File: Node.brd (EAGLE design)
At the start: 38.1 x 38.1 mm, 72 parts, among them J1 AVR_SPI_PRG_6NS, J2 M04X2, Q1 PMR280UN, Q2 PMR280UN, Q3 PMR280UN, U1 ATMEGA32U4, U2 BLUETOOTH-RN41", U4 L3GD20, U5 LTC3554, U6 LSM303DLHC, U9 RCLAMP0502A, X1 USBSMD

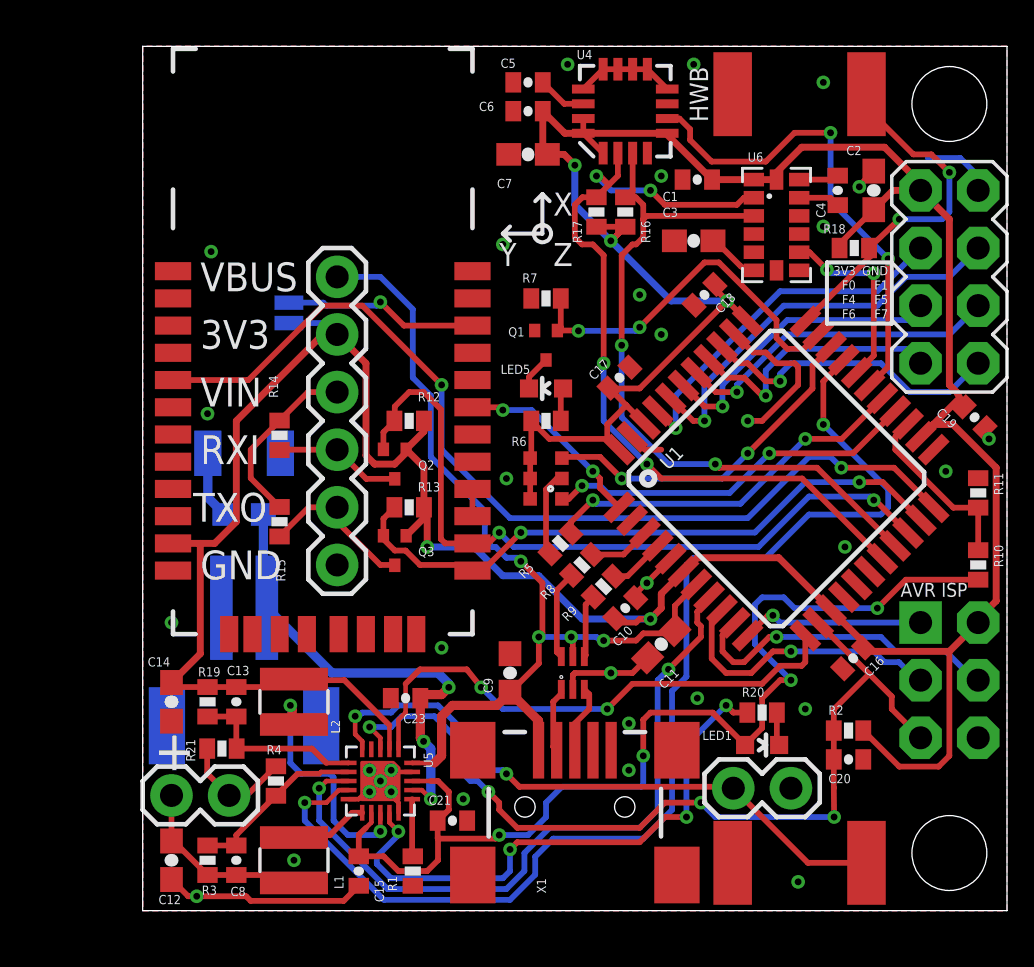
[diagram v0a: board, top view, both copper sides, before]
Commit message: cleanup for rev3 and use ltc3553
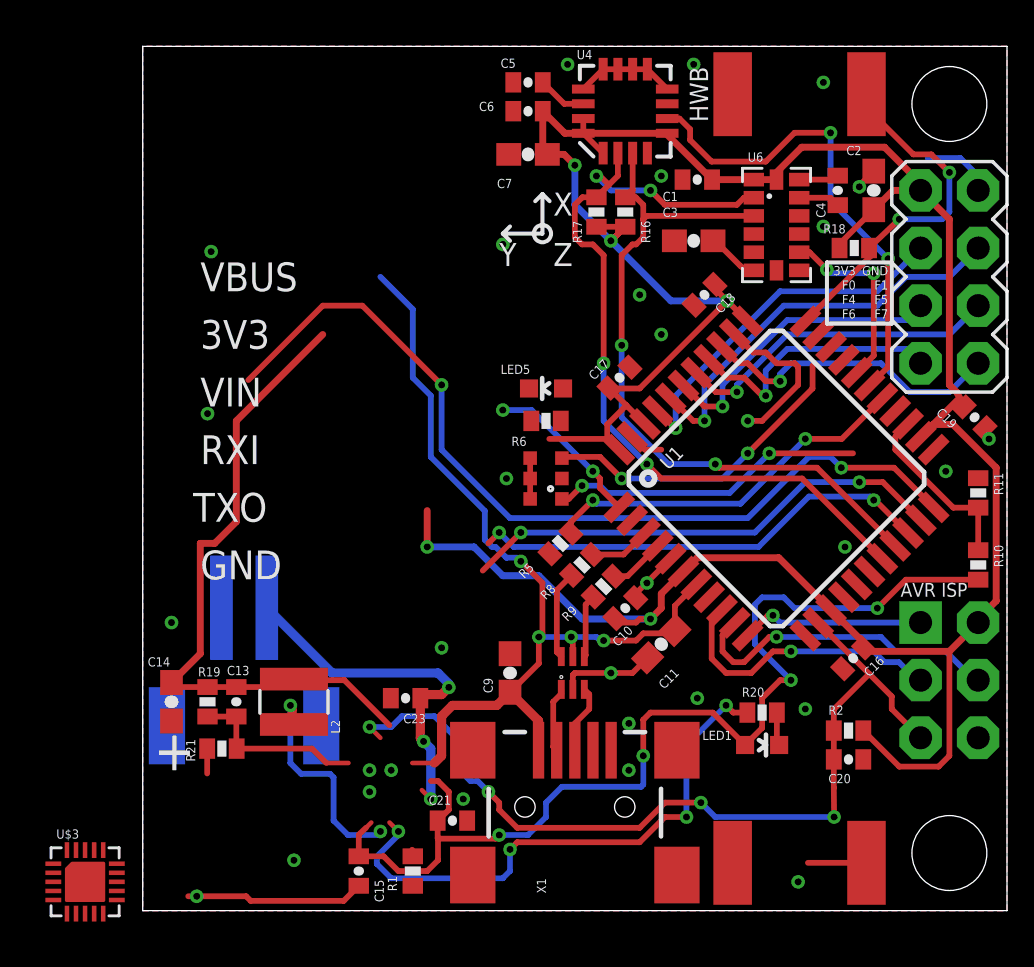
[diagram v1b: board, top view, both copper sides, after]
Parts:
- removed C12: 10uF, SparkFun:0603-CAP
- removed C22: 100uF, SparkFun:1210
- removed C8: 10pF, SparkFun:0402-CAP
- removed JP1: ON, SparkFun-Connectors:1X02
- removed JP2: UART, SparkFun:1X06
- removed JP3: 3V3, SparkFun-Connectors:1X02
- removed L1: 4.7uH, adjacent-reality:VLS30
- removed Q1, Q2, Q3: PMR280UN, adjacent-reality:SOT416
- removed R12, R13, R14, R15: 4.7k, SparkFun:0402-RES
- removed R22: 0.3, SparkFun:0603-RES
- removed R3: 2.05M, SparkFun:0402-RES
- removed R4: 649k, SparkFun:0402-RES
- removed R7: 1M, SparkFun:0402-RES
- removed SJ1: SOLDERJUMPERNO, SparkFun:SJ_2S-NO
- removed U2: BLUETOOTH-RN41", adjacent-reality:RN41
- removed U5: LTC3554, adjacent-reality:QFN20-3X3
- added U$3: LTC3553, adjacent-reality:QFN20-3X3
- R1: value 1.5k -> 7.5k
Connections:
- removed net HPWR: U1.12, U5.1
- removed net N$14: SJ1.1, U2.22
- removed net N$19: C12.1, C8.1, JP3.1, L1.2, R3.2
- removed net N$20: LED5.C, Q1.3
- removed net N$22: Q1.1, R7.2, U1.32
- removed net N$23: L1.1, U5.11
- removed net N$31: C8.2, R3.1, R4.2, U5.7
- removed net N$36: C22.1, R22.1
- removed net N$9 (its old number): U2.15, U2.16
- removed net PWR_ON1: U1.30, U5.9
- removed net PWR_ON2: U1.8, U5.8
- removed net RX_I: JP2.4, Q2.3, R14.1
- removed net TX_O: JP2.5, Q3.3, R15.1
- removed net VIN: JP2.3, R14.2, R15.2
- new net BUCK_ON: U$3.1
- new net N$10: LED5.C, R6.1
- new net STBY: U$3.6
- net +3V3: now also LED5.A; no longer JP2.2, Q2.1, Q3.1, R12.2, R13.2, R6.2, SJ1.2, U2.11, U5.2
- net GND: now also U$3.15, U$3.19, U$3.2, U$3.21, U$3.5; no longer C12.2, C22.2, JP1.2, JP2.6, JP3.2, Q1.2, R4.1, R7.1, U2.1, U2.12, U2.20, U2.28, U2.29, U2.3, U2.4, U5.10, U5.15, U5.19, U5.21
- net N$1: now also U$3.11, U$3.12, U$3.18; no longer U5.12, U5.18
- net N$12: now also U1.32; no longer U1.31
- net N$16: now also U$3.14; no longer U5.14
- net N$17: now also U1.30; no longer U1.26
- net N$2: now also U$3.16; no longer U5.16
- net N$27: now also U$3.13; no longer U5.13
- net N$29: now also U$3.17; no longer R22.2, U5.17
- net N$37: now also U$3.8; no longer U5.6
- net N$4: now also R6.2, U1.31; no longer LED5.A, R6.1
- net N$8: no longer JP1.1, U5.5
- net RBT: no longer U2.5
- net RESET: no longer U5.3
- net RX: no longer Q2.2, R12.1, U2.14
- net SBT: no longer U2.19
- net TX: no longer Q3.2, R13.1, U2.13
- net VBUS: now also U$3.20; no longer JP2.1, U5.20
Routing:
- net PWR_ON1: track 51.8 -> 0.00 mm, vias 2 -> 0
- net PWR_ON2: track 31.4 -> 0.00 mm, vias 2 -> 0
- net N$8: track 27.9 -> 2.58 mm, vias 2 -> 0
- net HPWR: track 23.7 -> 0.00 mm, vias 2 -> 0
- net +3V3: track 180.0 -> 157.6 mm
- net N$22: track 16.5 -> 0.00 mm, vias 2 -> 0
- net RX: track 33.2 -> 20.5 mm
- net GND: track 43.1 -> 33.1 mm, vias 33 -> 31
- net N$14: track 8.64 -> 0.00 mm, vias 1 -> 0
- net N$19: track 8.17 -> 0.00 mm
- net VIN: track 7.92 -> 0.00 mm
- net N$31: track 7.85 -> 0.00 mm
- net TX_O: track 7.04 -> 0.00 mm
- net TX: track 28.2 -> 21.6 mm
- net RX_I: track 5.62 -> 0.00 mm
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
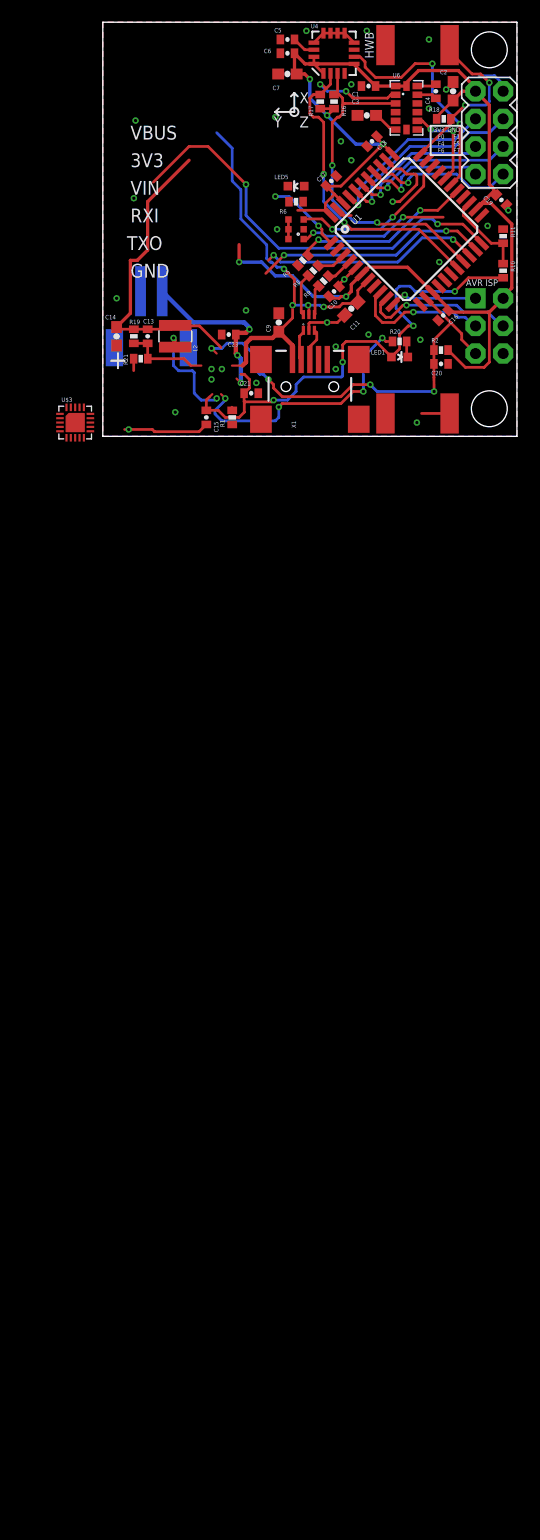
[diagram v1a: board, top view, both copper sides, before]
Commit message: add header and crystal
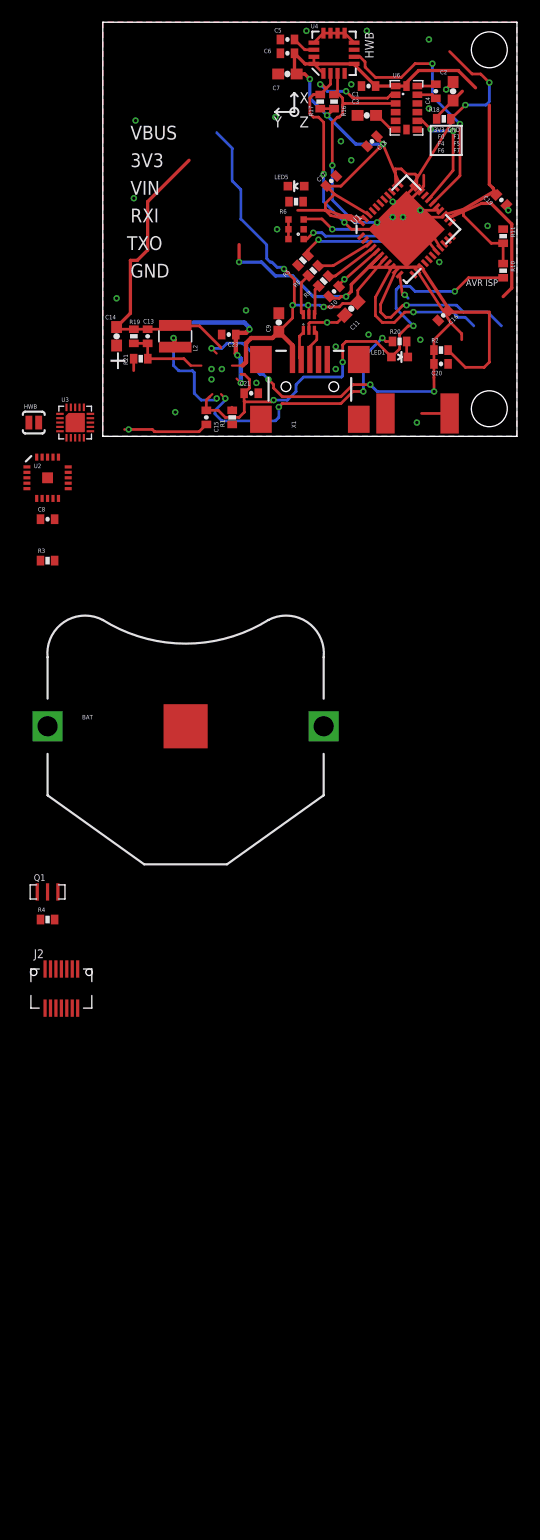
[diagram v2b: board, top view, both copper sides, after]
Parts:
- removed J1: AVR_SPI_PRG_6NS, SparkFun:2X3-NS
- added C8: 33nF, SparkFun:0402-CAP
- added Q1: 16MHz, adjacent-reality:PRQC
- added R3: 22k, SparkFun:0402-RES
- added R4: 1M, SparkFun:0402-RES
- added U2: NRF24L01SMD, SparkFun-RF:QFN20
- BAT: value JST -> (none); device SparkFun:JST-2-SMD -> SparkFun-Electromechanical:BATTCON_245MM_PTH
- HWB: value KSS -> SOLDERJUMPERNO; device adjacent-reality:KSS -> SparkFun-Passives:SJ_2S-NO
- J2: value M04X2 -> DF12A3.0-14DS; device SparkFun:2X4 -> adjacent-reality:DF12A3.0-14DS
- U1: value ATMEGA32U4 -> ATMEGA32U4QFN; device adjacent-reality:TQFP44 -> adjacent-reality:QFN-44
- moved J2 88.0 mm to (-3.81, -50.8), turned to 0 degrees
- moved HWB 49.5 mm to (-6.35, 1.27), turned to 0 degrees
- moved BAT 36.5 mm to (7.62, -26.7), flipped to the top, turned to 0 degrees
- renumbered U$3 to U3
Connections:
- removed net N$28: J2.1, U1.36
- removed net N$30: J2.2, U1.37
- removed net N$32: J2.3, U1.38
- removed net N$33: J2.4, U1.39
- removed net N$34: J2.5, U1.40
- removed net N$35: J2.6, U1.41
- removed net RBT: U1.22
- removed net SBT: U1.1
- new net A0: J2.9, U1.41
- new net A1: J2.10, U1.40
- new net A4: J2.11, U1.39
- new net A5: J2.12, U1.38
- new net A6: J2.13, U1.37
- new net A7: J2.14, U1.36
- new net CE: U1.1, U2.1
- new net N$11: C8.1, U2.19
- new net N$14: R3.2, U2.16
- new net N$19: Q1.P$1, R4.1, U2.9
- new net N$20: Q1.P$3, R4.2, U2.10
- new net PCINT7: U1.12, U2.6
- new net SS: U1.8, U2.2
- new net VDD_PA: U2.11
- net +3V3: now also J2.2, U2.15, U2.18, U2.7; no longer J1.2, J2.8
- net BUCK_ON: now also U1.22
- net GND: now also BAT.2, C8.2, HWB.1, J2.6, Q1.P$2, R3.1, U2.0, U2.14, U2.17, U2.20, U2.8; no longer BAT.1, HWB.P$2, J1.6, J2.7
- net HWB: now also HWB.2; no longer HWB.P$1
- net MISO: now also J2.1, U2.5; no longer J1.1
- net MOSI: now also J2.4, U2.4; no longer J1.4
- net N$29: now also BAT.3; no longer BAT.2
- net RESET: now also J2.5; no longer J1.5
- net RX: now also J2.7
- net SCK: now also J2.3, U2.3; no longer J1.3
- net STBY: now also U1.26
- net TX: now also J2.8
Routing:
- net RBT: track 39.2 -> 0.00 mm, vias 2 -> 0
- net TX: track 21.6 -> 0.00 mm, vias 2 -> 0
- net RX: track 20.5 -> 0.00 mm, vias 2 -> 0
- net N$34: track 18.1 -> 0.00 mm, vias 1 -> 0
- net N$35: track 16.0 -> 0.00 mm, vias 1 -> 0
- net N$32: track 14.5 -> 0.00 mm, vias 1 -> 0
- net +3V3: track 157.6 -> 171.9 mm
- net N$28: track 13.5 -> 0.00 mm, vias 1 -> 0
- net N$33: track 13.2 -> 0.00 mm, vias 1 -> 0
- net N$30: track 11.7 -> 0.00 mm, vias 1 -> 0
- net SBT: track 7.34 -> 0.00 mm, vias 2 -> 0
- net MISO: track 8.13 -> 2.54 mm
- net N$29: track 16.4 -> 12.2 mm
- net N$15: track 2.71 -> 5.21 mm
- net MOSI: track 14.2 -> 16.7 mm
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
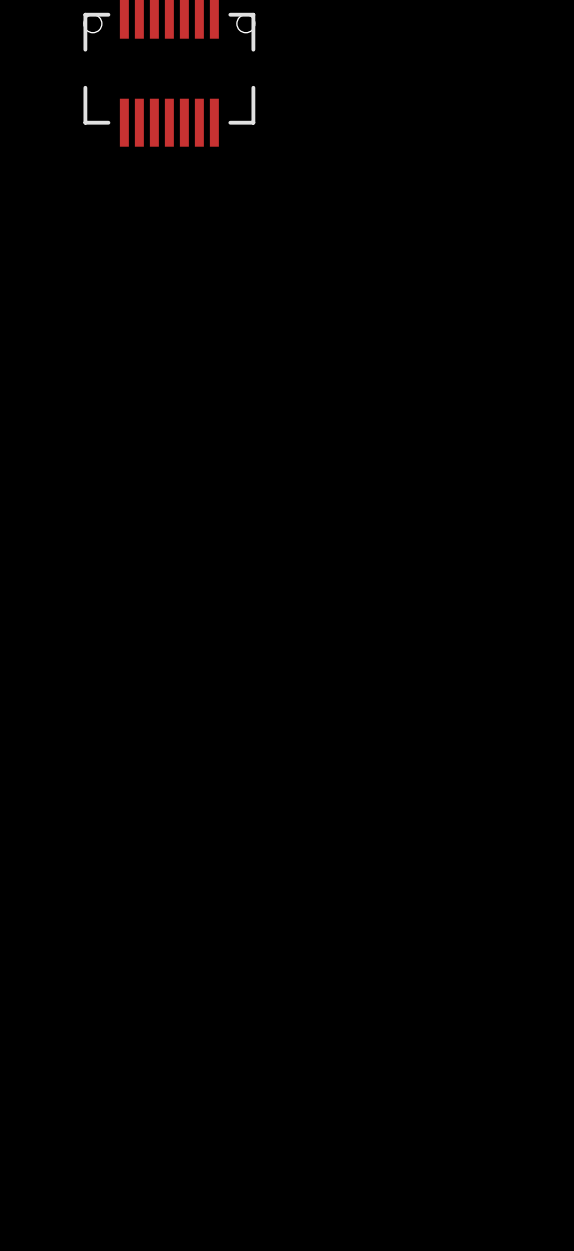
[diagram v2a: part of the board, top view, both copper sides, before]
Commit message: balun for nrf24l01
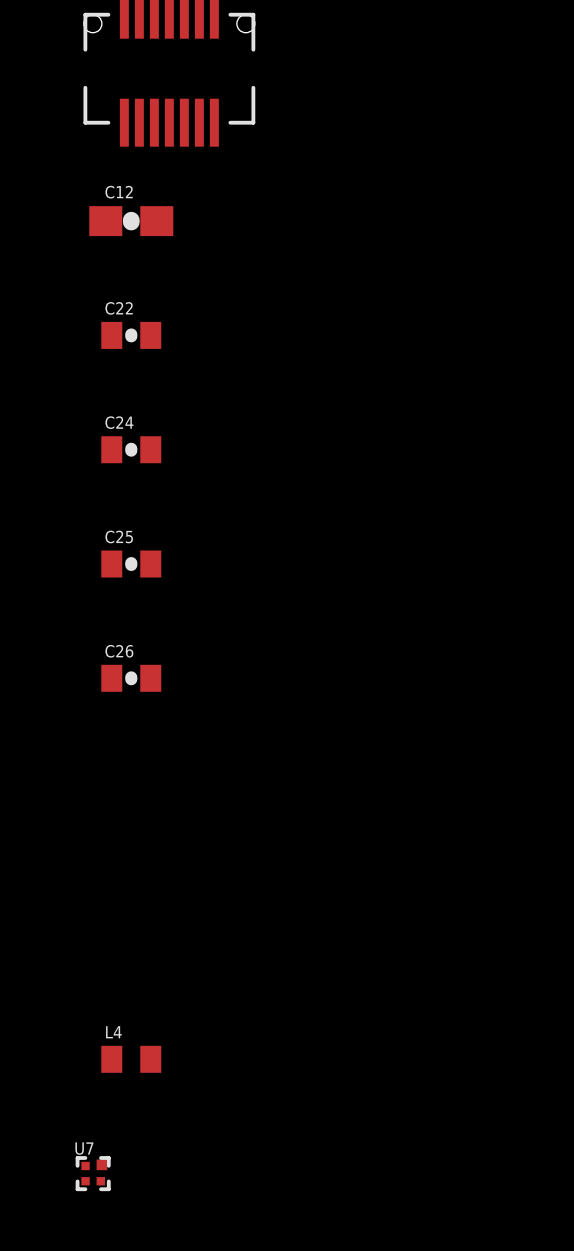
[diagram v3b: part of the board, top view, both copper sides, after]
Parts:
- added C12: 10uF, SparkFun:0603-CAP
- added C22: 10nF, SparkFun:0402-CAP
- added C24: 1nF, SparkFun:0402-CAP
- added C25: 2.2nF, SparkFun:0402-CAP
- added C26: 4.7pF, SparkFun:0402-CAP
- added L4: 3.9nH, adjacent-reality:C0402
- added U7: BD2425NNRF0404, adjacent-reality:BD2425NNRF
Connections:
- removed net VDD_PA: U2.11
- new net N$21: U2.13, U7.3
- new net N$22: U2.12, U7.4
- new net N$23: C25.1, C26.1, U2.11, U7.1
- new net N$28: L4.1, U7.2
- new net VSS: U2.0
- net +3V3: now also C12.1, C22.1, C24.1
- net GND: now also C12.2, C22.2, C24.2, C25.2, C26.2; no longer U2.0

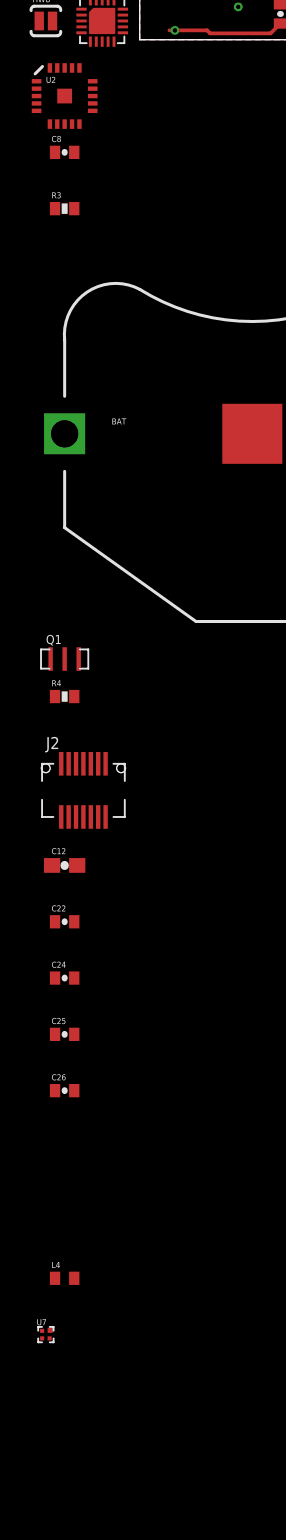
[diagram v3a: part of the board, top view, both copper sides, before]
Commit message: add the antenna
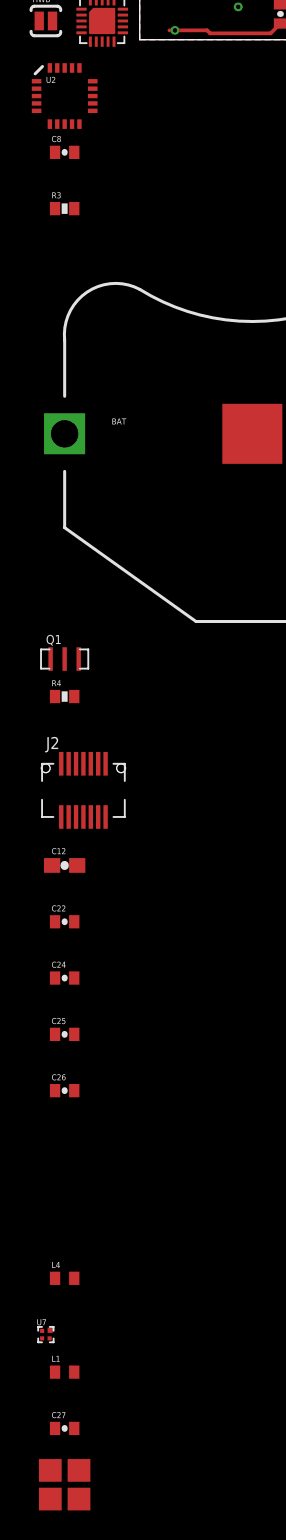
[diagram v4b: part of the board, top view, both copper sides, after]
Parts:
- added C27: TBD, SparkFun:0402-CAP
- added L1: TBD, adjacent-reality:C0402
- added RF: ANTENNA2MOLEX, adjacent-reality:MOLEX2.4SMD
- U2: value NRF24L01SMD -> NRF24L01NOPAD; device SparkFun-RF:QFN20 -> adjacent-reality:QFN20-NOPAD
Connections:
- removed net VSS: U2.0
- new net N$30: L1.2, RF.FEED
- new net N$31: C27.1, L1.1, L4.2
- net GND: now also C27.2
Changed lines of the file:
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@@
 <element name="U3" library="adjacent-reality" package="QFN20-3X3" value="LTC3553" x="-2.54" y="1.27"/>
 <element name="HWB" library="SparkFun-Passives" package="SJ_2S-NO" value="SOLDERJUMPERNO" x="-6.35" y="1.27"/>
-<element name="U2" library="SparkFun-RF" package="QFN20" value="NRF24L01SMD" x="-5.08" y="-3.81"/>
+<element name="U2" library="adjacent-reality" package="QFN20-NOPAD" value="NRF24L01NOPAD" x="-5.08" y="-3.81"/>
 <element name="C8" library="SparkFun" package="0402-CAP" value="33nF" x="-5.08" y="-7.62"/>
 <element name="R3" library="SparkFun" package="0402-RES" value="22k" x="-5.08" y="-11.43"/>
@@
 <element name="L4" library="adjacent-reality" package="C0402" value="3.9nH" x="-5.08" y="-83.82"/>
 <element name="U7" library="adjacent-reality" package="BD2425NNRF" value="BD2425NNRF0404" x="-6.35" y="-87.63"/>
+<element name="L1" library="adjacent-reality" package="C0402" value="TBD" x="-5.08" y="-90.17"/>
+<element name="C27" library="SparkFun" package="0402-CAP" value="TBD" x="-5.08" y="-93.98"/>
+<element name="RF" library="adjacent-reality" package="MOLEX2.4SMD" value="ANTENNA2MOLEX" x="-5.08" y="-97.79"/>
 </elements>
 <signals>
@@
 <contactref element="C25" pad="2"/>
 <contactref element="C26" pad="2"/>
+<contactref element="C27" pad="2"/>
+<wire x1="-4.43" y1="-71.12" x2="-4.43" y2="-93.98" width="0" layer="19" extent="1-1"/>
 <wire x1="-4.43" y1="-67.31" x2="-4.43" y2="-71.12" width="0" layer="19" extent="1-1"/>
 <wire x1="-4.43" y1="-63.5" x2="-4.43" y2="-67.31" width="0" layer="19" extent="1-1"/>
@@
 </signal>
 <signal name="VSS">
-<contactref element="U2" pad="0"/>
+</signal>
+<signal name="N$31">
+<contactref element="L4" pad="2"/>
+<contactref element="C27" pad="1"/>
+<contactref element="L1" pad="1"/>
+<wire x1="-5.73" y1="-90.17" x2="-5.73" y2="-93.98" width="0" layer="19" extent="1-1"/>
+<wire x1="-4.43" y1="-83.82" x2="-5.73" y2="-90.17" width="0" layer="19" extent="1-1"/>
+</signal>
+<signal name="N$30">
+<contactref element="L1" pad="2"/>
+<contactref element="RF" pad="FEED"/>
+<wire x1="-4.43" y1="-90.17" x2="-4.11" y2="-98.76" width="0" layer="19" extent="1-1"/>
 </signal>
 </signals>
